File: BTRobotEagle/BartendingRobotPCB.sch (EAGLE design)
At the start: 34 parts, among them P1 B2B-XH-A(LF)(SN), P10 B2B-XH-A(LF)(SN), P11 B2B-XH-A(LF)(SN), P2 B2B-XH-A(LF)(SN), P3 B2B-XH-A(LF)(SN), P4 B2B-XH-A(LF)(SN), P5 B2B-XH-A(LF)(SN), P6 B2B-XH-A(LF)(SN), P7 B2B-XH-A(LF)(SN), P8 B2B-XH-A(LF)(SN), P9 B2B-XH-A(LF)(SN)

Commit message: update brd/sch
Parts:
- added C3, C4: 10MMCAP, BartendingRobot:10MMCAP
- added MGT1, MGT2, MGT3, MGT4, MGT5, MGT6, MGT7, MGT8: MOUNTING_HOLE, BartendingRobot:MOUNTING_HOLE
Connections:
- net 12V: now also C3.P, C4.P
- net CGND: now also C3.N, C4.N, MGT1.P$1, MGT2.P$1, MGT3.P$1, MGT4.P$1, MGT5.P$1, MGT6.P$1, MGT7.P$1, MGT8.P$1
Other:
- note added: "12V Motor Controller"
- note added: "Endstop Headers"
- note added: "GPIO Exanders"
- note added: "Mounting Holes"
- note added: "Power Converters"
- note added: "Pump Controllers and Headers"
- note added: "Raspberry Pi"
- note added: "Stepper Controllers and Headers"
- moved on the sheet: PI

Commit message: more changes
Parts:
- added C5, C6, C7: SMALLCAP, BartendingRobot:SMALLCAP
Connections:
- net 12V: now also C5.P; no longer C3.P, C4.P
- net 5V: now also C3.P, C7.P
- net 8.6V: now also C4.P, C6.P
- net CGND: now also C5.N, C6.N, C7.N
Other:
- moved on the sheet: 1K, 5V, 8.6V, C3, C4, SP1

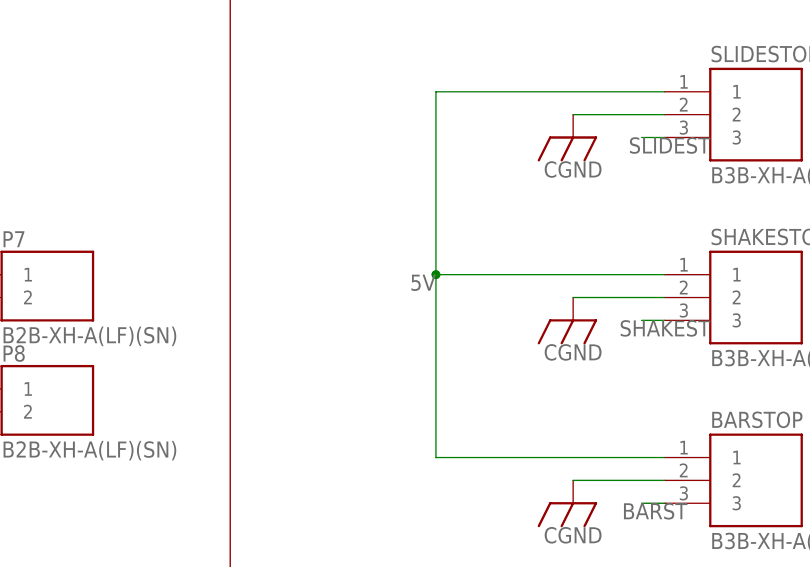
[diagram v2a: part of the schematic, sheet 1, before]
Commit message: finish power and ground traces
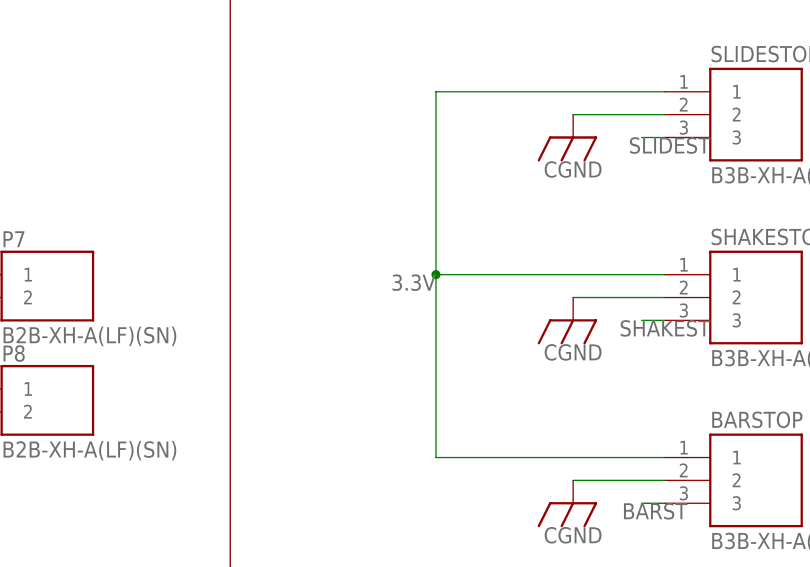
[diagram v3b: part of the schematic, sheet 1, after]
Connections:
- net 3.3V: now also BARSTOP.1, SHAKESTOP.1, SLIDESTOP.1
- net 5V: no longer BARSTOP.1, SHAKESTOP.1, SLIDESTOP.1
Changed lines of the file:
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@@
 <junction x="365.76" y="55.88"/>
-</segment>
-<segment>
-<pinref part="SLIDESTOP" gate="G$1" pin="1"/>
-<wire x1="223.52" y1="149.86" x2="198.12" y2="149.86" width="0.1524" layer="91"/>
-<wire x1="198.12" y1="149.86" x2="198.12" y2="129.54" width="0.1524" layer="91"/>
-<pinref part="BARSTOP" gate="G$1" pin="1"/>
-<wire x1="198.12" y1="129.54" x2="198.12" y2="109.22" width="0.1524" layer="91"/>
-<wire x1="198.12" y1="109.22" x2="223.52" y2="109.22" width="0.1524" layer="91"/>
-<pinref part="SHAKESTOP" gate="G$1" pin="1"/>
-<wire x1="223.52" y1="129.54" x2="198.12" y2="129.54" width="0.1524" layer="91"/>
-<junction x="198.12" y="129.54"/>
-<label x="198.12" y="129.54" size="1.778" layer="95" rot="R180"/>
 </segment>
 </net>
@@
 <label x="284.48" y="193.04" size="1.778" layer="95" rot="R180"/>
 </segment>
+<segment>
+<pinref part="SLIDESTOP" gate="G$1" pin="1"/>
+<wire x1="223.52" y1="149.86" x2="198.12" y2="149.86" width="0.1524" layer="91"/>
+<wire x1="198.12" y1="149.86" x2="198.12" y2="129.54" width="0.1524" layer="91"/>
+<pinref part="BARSTOP" gate="G$1" pin="1"/>
+<wire x1="198.12" y1="129.54" x2="198.12" y2="109.22" width="0.1524" layer="91"/>
+<wire x1="198.12" y1="109.22" x2="223.52" y2="109.22" width="0.1524" layer="91"/>
+<pinref part="SHAKESTOP" gate="G$1" pin="1"/>
+<wire x1="223.52" y1="129.54" x2="198.12" y2="129.54" width="0.1524" layer="91"/>
+<junction x="198.12" y="129.54"/>
+<label x="198.12" y="129.54" size="1.778" layer="95" rot="R180"/>
+</segment>
 </net>
